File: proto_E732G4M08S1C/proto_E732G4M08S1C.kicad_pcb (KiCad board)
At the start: 2 copper layers, 14.5 x 6.2 mm, 10 parts, among them J1 USB4510-03-1-A, U1 FUSB302B01MPX, U2 SRV05-4

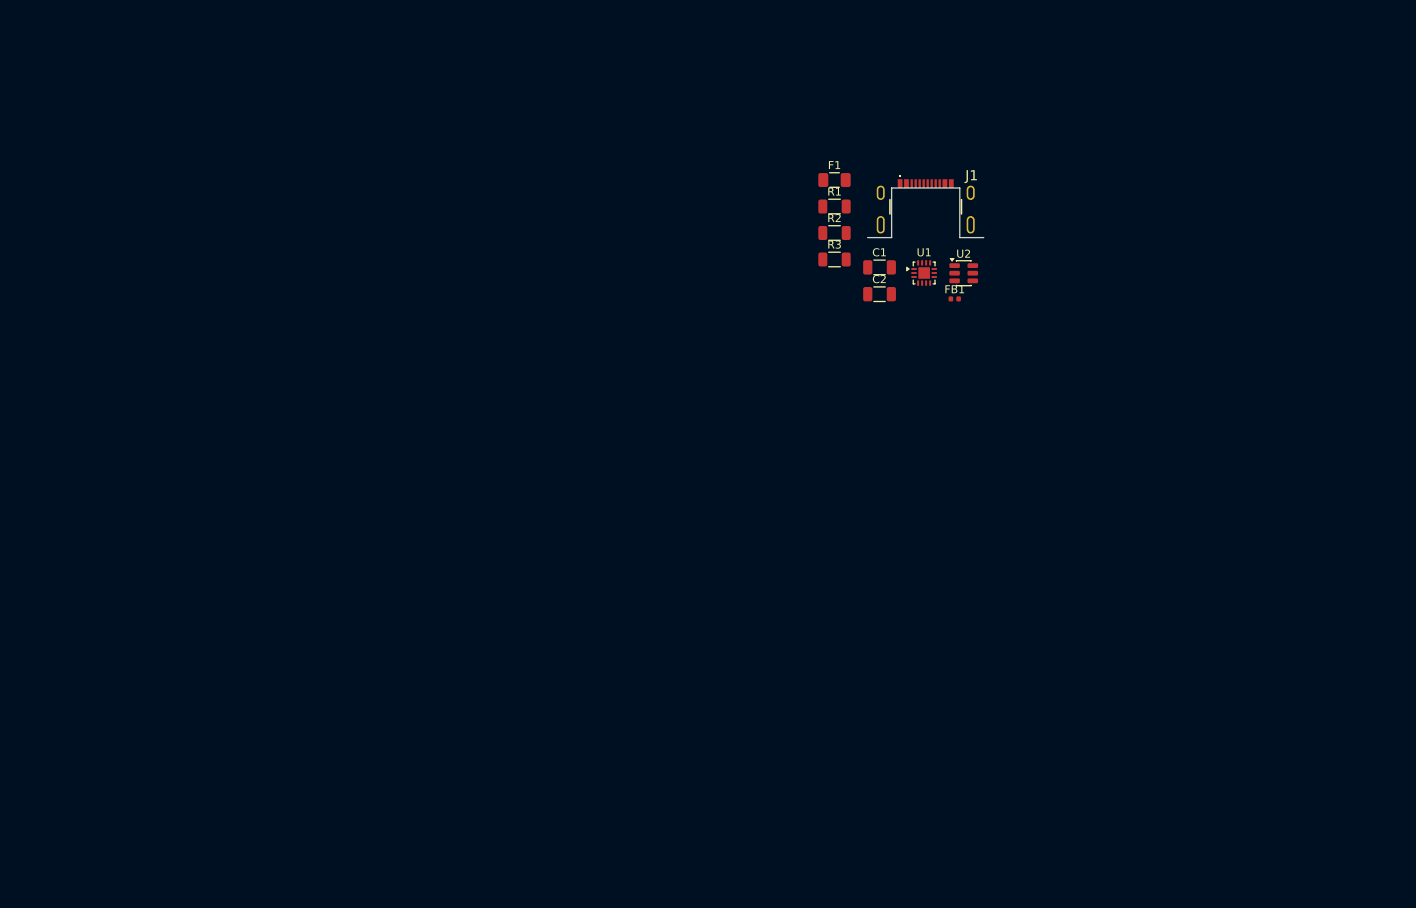
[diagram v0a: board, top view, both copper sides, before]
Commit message: feat(pcb) initial blocks and MCU
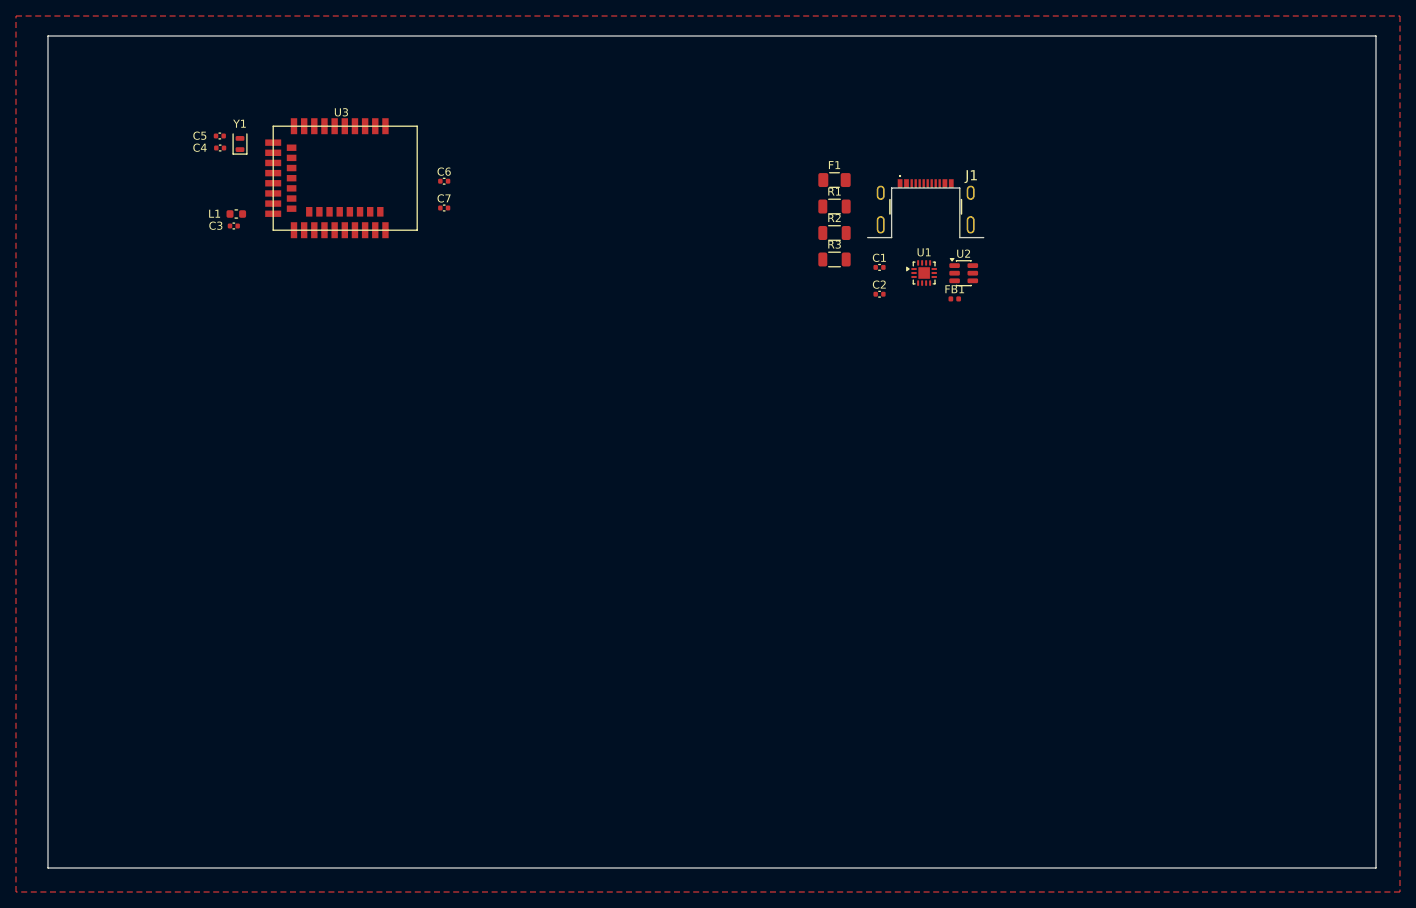
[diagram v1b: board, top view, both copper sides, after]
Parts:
- added C3: 1uF, Capacitor_SMD:C_0402_1005Metric, F.Cu at (90.7, 62.8)
- added C4: 12pF, Capacitor_SMD:C_0402_1005Metric, F.Cu at (89.0, 53.0)
- added C5: 12pF, Capacitor_SMD:C_0402_1005Metric, F.Cu at (89.0, 51.5)
- added C6: 4.7uF, Capacitor_SMD:C_0402_1005Metric, F.Cu at (117.0, 57.1)
- added C7: 4.7uF, Capacitor_SMD:C_0402_1005Metric, F.Cu at (117.0, 60.5)
- added L1: 10uH, Inductor_SMD:L_0603_1608Metric, F.Cu at (91.0, 61.2)
- added U3: E73-2G4M08S1C, stellar:E73(2G4M08S1C), F.Cu at (95.7, 63.3)
- added Y1: 32.768 kHz, Crystal:Crystal_SMD_2012-2Pin_2.0x1.2mm, F.Cu at (91.5, 52.5)
- C1, C2: footprint Capacitor_SMD:C_1206_3216Metric -> Capacitor_SMD:C_0402_1005Metric
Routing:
- added copper zone on F.Cu, net GND
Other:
- board size 14.5 x 6.2 mm -> 166 x 104 mm

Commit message: chg(pcb) more MCU and usb
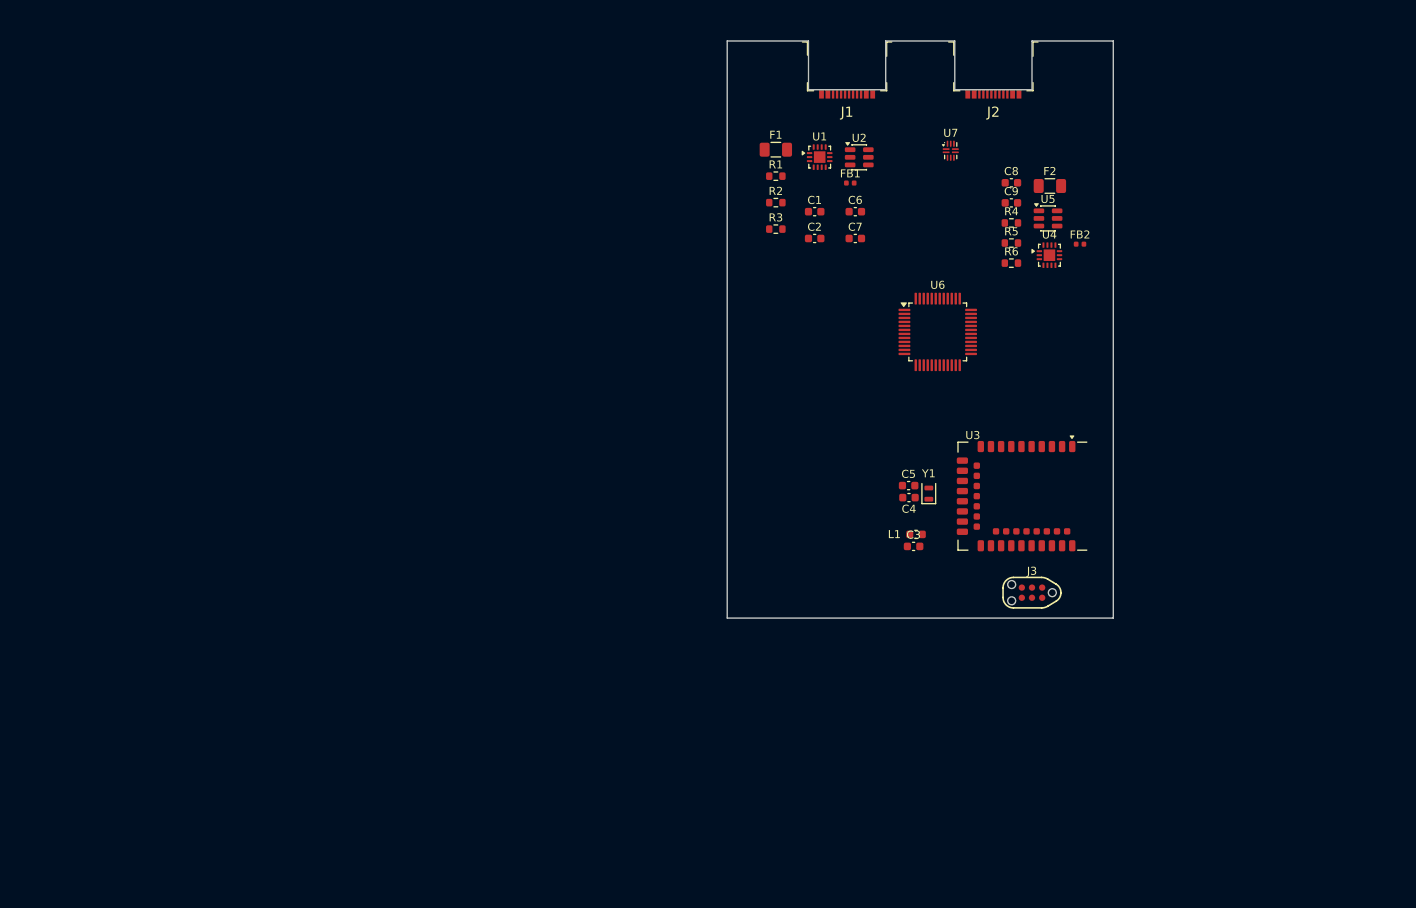
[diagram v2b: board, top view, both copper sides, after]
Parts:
- added C8: 100nF, Capacitor_SMD:C_0603_1608Metric, F.Cu at (187.9, 57.4)
- added C9: 1uF, Capacitor_SMD:C_0603_1608Metric, F.Cu at (187.9, 59.9)
- added F2: 3.0A 1206 Polyfuse, Fuse:Fuse_1206_3216Metric, F.Cu at (192.7, 57.8)
- added FB2: BLM15PX121SN1D, Inductor_SMD:L_0402_1005Metric, F.Cu at (196.5, 65.0)
- added J2: USB_C_Receptacle_USB2.0_16P, stellar:USB4510031A, F.Cu at (185.7, 45.7)
- added J3: TC2030_SWD, PCM_marbastlib-various:CON_TC2030_outlined, F.Cu at (190.5, 108.6)
- added R4: 4k7, Resistor_SMD:R_0603_1608Metric, F.Cu at (187.9, 62.4)
- added R5: 4k7, Resistor_SMD:R_0603_1608Metric, F.Cu at (187.9, 64.9)
- added R6: 4k7, Resistor_SMD:R_0603_1608Metric, F.Cu at (187.9, 67.4)
- added U4: FUSB302B01MPX, Package_DFN_QFN:WQFN-14-1EP_2.5x2.5mm_P0.5mm_EP1.45x1.45mm, F.Cu at (192.7, 66.4)
- added U5: SRV05-4, Package_TO_SOT_SMD:SOT-23-6, F.Cu at (192.5, 61.8)
- added U6: FE1.1, Package_QFP:LQFP-48_7x7mm_P0.5mm, F.Cu at (178.7, 76.0)
- added U7: PI3USB102EZLEX, Package_DFN_QFN:UQFN-10_1.3x1.8mm_P0.4mm, F.Cu at (180.3, 53.3)
- C1, C2, C3, C4, C5, C6, C7: footprint Capacitor_SMD:C_0402_1005Metric -> Capacitor_SMD:C_0603_1608Metric
- R1, R2, R3: footprint Resistor_SMD:R_1206_3216Metric -> Resistor_SMD:R_0603_1608Metric
- U3: value E73-2G4M08S1C -> nRF52840_E73-2G4M08S1C; footprint stellar:E73(2G4M08S1C) -> PCM_marbastlib-various:nRF52840_E73-2G4M08S1C
- moved U3 100.5 mm to (190.5, 96.5), turned to -90 degrees
- moved C4 96.6 mm to (175.1, 96.7)
- moved C5 96.6 mm to (175.1, 95.2)
- moved Y1 96.6 mm to (177.6, 96.2)
- moved L1 93.9 mm to (176.0, 101.3)
- moved C3 93.9 mm to (175.7, 102.8)
- moved C6 51.5 mm to (168.4, 61.0)
- moved C7 51.5 mm to (168.4, 64.3)
- moved U2 19.5 mm to (168.9, 54.2)
- moved U1 19.5 mm to (164.0, 54.1)
- moved FB1 19.5 mm to (167.8, 57.4)
- moved J1 18.5 mm to (167.4, 45.7)
- moved C2 10.7 mm to (163.3, 64.3)
- moved C1 10.7 mm to (163.3, 61.0)
- moved F1 8.26 mm to (158.5, 53.2)
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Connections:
- C3 pad 1: +3.3V -> VDD
- L1 pad 1: +3.3V -> DCCH
- L1 pad 2: Net-(U3A-DCCH) -> VDD
- U3 pad 19: unconnected-(U3A-VDD-Pad19) -> VDD
- U3 pad 21: unconnected-(U3A-GND-Pad21) -> GND
- U3 pad 23: unconnected-(U3A-VDDH-Pad23) -> VCC
- U3 pad 24: unconnected-(U3A-GND-Pad24) -> GND
- U3 pad 25: Net-(U3A-DCCH) -> DCCH
- U3 pad 26: Net-(U3A-P0.18/RESET) -> /MCU nRF52840/RST
- U3 pad 37: unconnected-(U3A-SWDIO-Pad37) -> /MCU nRF52840/SWCLK
- U3 pad 39: unconnected-(U3A-SWDCLK-Pad39) -> /MCU nRF52840/SWDIO
- U3 pad 5: unconnected-(U3A-GND-Pad5) -> GND
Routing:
- removed copper zone on F.Cu, net GND
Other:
- board size 166 x 104 mm -> 48.3 x 72.1 mm

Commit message: feat(pcb) more changes
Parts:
- added C10: C, Capacitor_SMD:C_0603_1608Metric, F.Cu at (156.1, 74.8)
- added C11: 4.7uF, Capacitor_SMD:C_0603_1608Metric, F.Cu at (156.1, 77.4)
- added C12: 4.7uF, Capacitor_SMD:C_0603_1608Metric, F.Cu at (156.1, 79.9)
- added Q1: 2N7002, Package_TO_SOT_SMD:SOT-23, F.Cu at (164.6, 81.3)
- added R10: 1k5, Resistor_SMD:R_0603_1608Metric, F.Cu at (160.2, 74.8)
- added R11: 10k, Resistor_SMD:R_0603_1608Metric, F.Cu at (160.2, 77.4)
- added R12: 100k, Resistor_SMD:R_0603_1608Metric, F.Cu at (160.2, 79.9)
- added R13: 10k, Resistor_SMD:R_0603_1608Metric, F.Cu at (160.2, 82.4)
- added R14: 100R, Resistor_SMD:R_0603_1608Metric, F.Cu at (160.2, 84.9)
- added R7: 47k, Resistor_SMD:R_0603_1608Metric, F.Cu at (156.1, 82.4)
- added R8: R, Resistor_SMD:R_0603_1608Metric, F.Cu at (156.1, 84.9)
- added R9: R, Resistor_SMD:R_0603_1608Metric, F.Cu at (156.1, 87.4)
- added U8: BQ24075RGT, Package_DFN_QFN:VQFN-16-1EP_3x3mm_P0.5mm_EP1.6x1.6mm, F.Cu at (164.8, 76.2)
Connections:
- net VCC renamed +VSW
